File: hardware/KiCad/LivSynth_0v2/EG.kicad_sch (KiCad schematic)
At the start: 27 parts, among them J11 Jumper, Q10 2N3904, Q13 2N3904, Q15 2N3904, Q2 2N3904, SW2 SW_SPST, U5 TL074

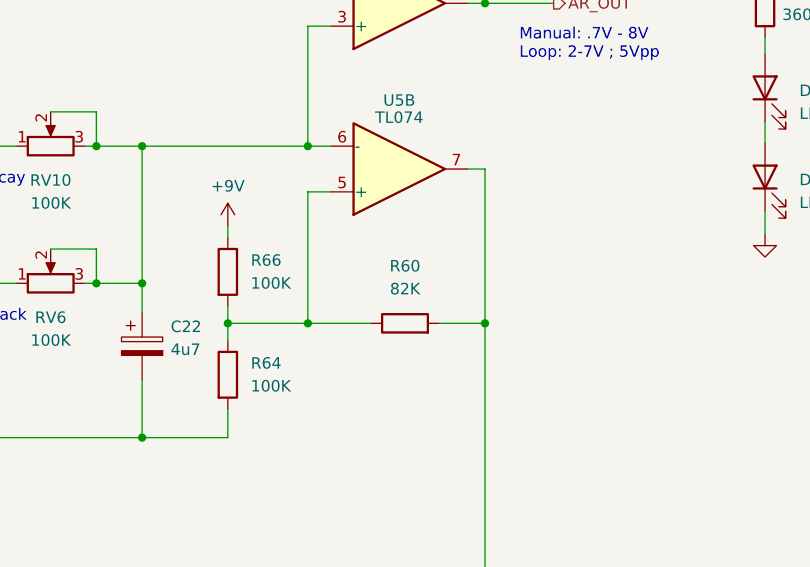
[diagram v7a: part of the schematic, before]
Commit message: EG: raise Rf of comparator circuit to improve performance LFO: raise coupling resistor for higher amplitude, adapt cap for more musical ranges
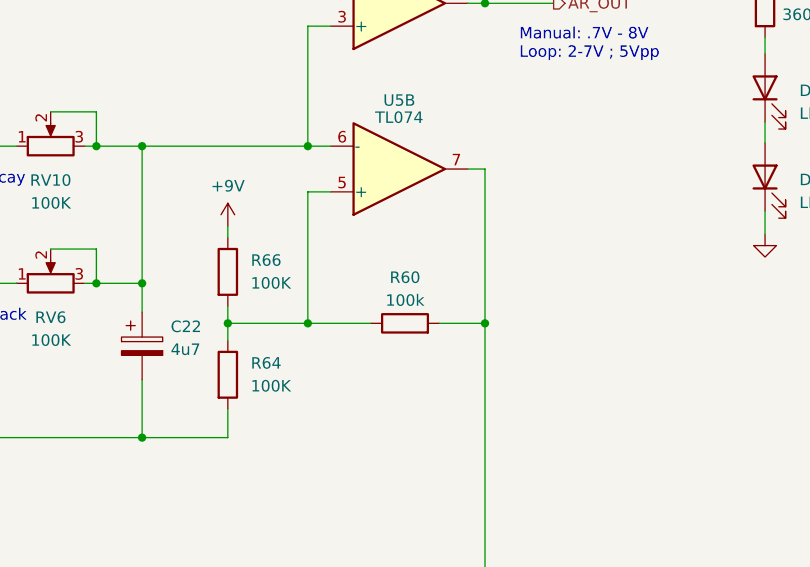
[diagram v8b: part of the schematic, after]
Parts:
- R60: value 82K -> 100k
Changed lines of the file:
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@@
   (symbol (lib_id "Device:R") (at 202.565 107.95 90) (unit 1)
     (in_bom yes) (on_board yes) (dnp no) (fields_autoplaced)
-    (property "Reference" "R60" (at 202.565 101.6 90)
+    (property "Reference" "R60" (at 202.565 102.87 90)
       (effects (font (size 1.27 1.27)))
     )
-    (property "Value" "82K" (at 202.565 104.14 90)
+    (property "Value" "100k" (at 202.565 105.41 90)
       (effects (font (size 1.27 1.27)))
     )
